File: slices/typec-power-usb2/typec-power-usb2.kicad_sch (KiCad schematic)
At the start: 8 parts, among them J2 USB_C_Receptacle_USB2.0_16P, U2 SMBJ5.0CA, U3 SMBJ5.0CA, U4 SMBJ5.0CA

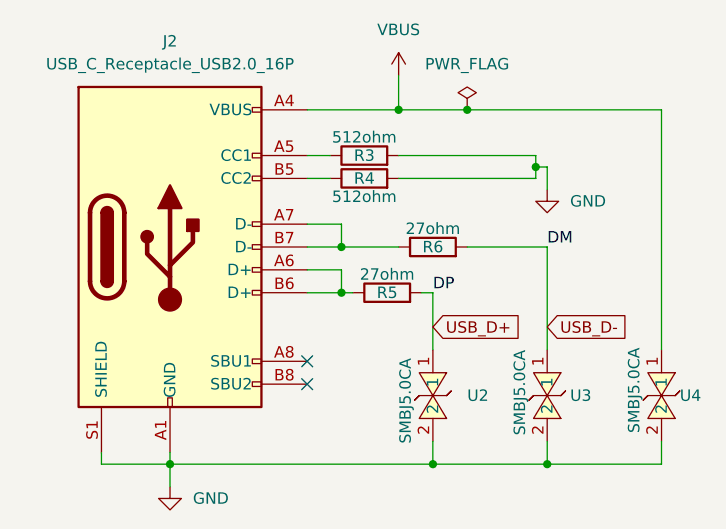
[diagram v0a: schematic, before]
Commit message: Add schematic for module `tlv62569`
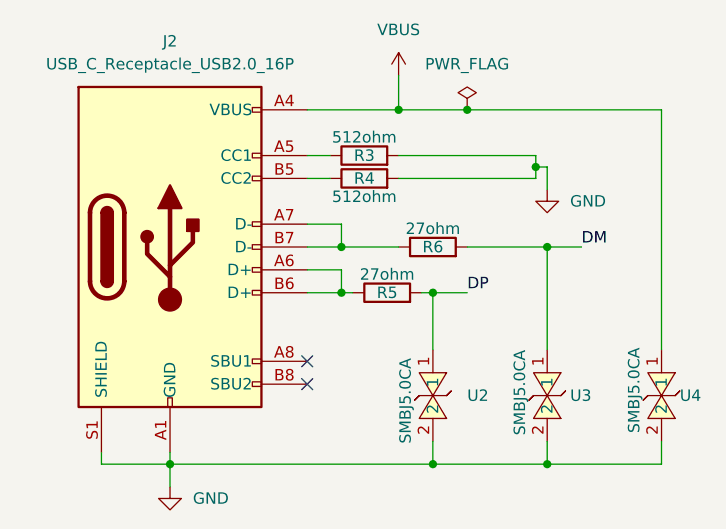
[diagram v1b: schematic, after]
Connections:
- net USB_D+ renamed DP
- net USB_D- renamed DM
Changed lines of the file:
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@@
+	)
+	(junction
+		(at 148.59 93.98)
+		(diameter 0)
+		(color 0 0 0 0)
+	)
+	(junction
+		(at 161.29 88.9)
+		(diameter 0)
+		(color 0 0 0 0)
 	)
 	(junction
@@
 	(wire
 		(pts
+			(xy 161.29 88.9) (xy 165.1 88.9)
+		)
+		(stroke
+			(width 0)
+			(type default)
+		)
+	)
+	(wire
+		(pts
 			(xy 161.29 80.01) (xy 160.02 80.01)
 		)
@@
 	(wire
 		(pts
+			(xy 148.59 93.98) (xy 152.4 93.98)
+		)
+		(stroke
+			(width 0)
+			(type default)
+		)
+	)
+	(wire
+		(pts
 			(xy 134.62 91.44) (xy 138.43 91.44)
 		)
@@
 	)
 	(label "DM"
-		(at 161.29 88.9 0)
+		(at 165.1 88.9 0)
 		(fields_autoplaced yes)
 		(effects
@@
 	)
 	(label "DP"
-		(at 148.59 93.98 0)
+		(at 152.4 93.98 0)
 		(fields_autoplaced yes)
 		(effects
@@
 			)
 			(justify left bottom)
-		)
-	)
-	(global_label "USB_D+"
-		(shape input)
-		(at 148.59 97.79 0)
-		(fields_autoplaced yes)
-		(effects
-			(font
-				(size 1.27 1.27)
-			)
-			(justify left)
-		)
-		(property "Intersheetrefs" "${INTERSHEET_REFS}"
-			(at 159.1952 97.79 0)
-			(effects
-				(font
-					(size 1.27 1.27)
-				)
-				(justify left)
-				(hide yes)
-			)
-		)
-	)
-	(global_label "USB_D-"
-		(shape input)
-		(at 161.29 97.79 0)
-		(fields_autoplaced yes)
-		(effects
-			(font
-				(size 1.27 1.27)
-			)
-			(justify left)
-		)
-		(property "Intersheetrefs" "${INTERSHEET_REFS}"
-			(at 171.8952 97.79 0)
-			(effects
-				(font
-					(size 1.27 1.27)
-				)
-				(justify left)
-				(hide yes)
-			)
 		)
 	)
@@
 		)
 		(instances
-			(project "typec"
+			(project "typec-power-usb2"
 				(path "/c5ec9cb7-a70c-486e-b21d-0f6f21bc1a22"
 					(reference "R5")
@@
 		)
 		(instances
-			(project "typec"
+			(project "typec-power-usb2"
 				(path "/c5ec9cb7-a70c-486e-b21d-0f6f21bc1a22"
 					(reference "U3")
@@
 		)
 		(instances
-			(project "typec"
+			(project "typec-power-usb2"
 				(path "/c5ec9cb7-a70c-486e-b21d-0f6f21bc1a22"
 					(reference "U4")
@@
 		)
 		(instances
-			(project "typec"
+			(project "typec-power-usb2"
 				(path "/c5ec9cb7-a70c-486e-b21d-0f6f21bc1a22"
 					(reference "J2")
@@
 		)
 		(instances
-			(project "typec"
+			(project "typec-power-usb2"
 				(path "/c5ec9cb7-a70c-486e-b21d-0f6f21bc1a22"
 					(reference "R6")
@@
 		)
 		(instances
-			(project "typec"
+			(project "typec-power-usb2"
 				(path "/c5ec9cb7-a70c-486e-b21d-0f6f21bc1a22"
 					(reference "R3")
@@
 		)
 		(instances
-			(project "typec"
+			(project "typec-power-usb2"
 				(path "/c5ec9cb7-a70c-486e-b21d-0f6f21bc1a22"
 					(reference "#PWR06")
@@
 		)
 		(instances
-			(project "typec"
+			(project "typec-power-usb2"
 				(path "/c5ec9cb7-a70c-486e-b21d-0f6f21bc1a22"
 					(reference "R4")
@@
 		)
 		(instances
-			(project "typec"
+			(project "typec-power-usb2"
 				(path "/c5ec9cb7-a70c-486e-b21d-0f6f21bc1a22"
 					(reference "#PWR07")
@@
 		)
 		(instances
-			(project "typec"
+			(project "typec-power-usb2"
 				(path "/c5ec9cb7-a70c-486e-b21d-0f6f21bc1a22"
 					(reference "#PWR08")
@@
 		)
 		(instances
-			(project "typec"
+			(project "typec-power-usb2"
 				(path "/c5ec9cb7-a70c-486e-b21d-0f6f21bc1a22"
 					(reference "#FLG02")

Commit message: Update signature of all schematics
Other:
- company: Krysztal Huang -> Krysztal Huang <krysztal.huang@outlook.com>
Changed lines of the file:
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@@
 		(title "TypeC Power Supplier with USB2.0 Support")
 		(date "2024-09-01")
-		(company "Krysztal Huang")
+		(company "Krysztal Huang <krysztal.huang@outlook.com>")
 	)
 	(junction
